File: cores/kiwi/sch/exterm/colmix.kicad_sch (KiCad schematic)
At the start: 9 parts

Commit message: issue#46
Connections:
- net H1B renamed H1_BUF
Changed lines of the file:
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@@
     (effects (font (size 1.27 1.27)) (justify right))
   )
-  (hierarchical_label "H1B" (shape input) (at 149.86 107.95 180)
+  (hierarchical_label "H1_BUF" (shape input) (at 149.86 107.95 180)
     (effects (font (size 1.27 1.27)) (justify right))
   )

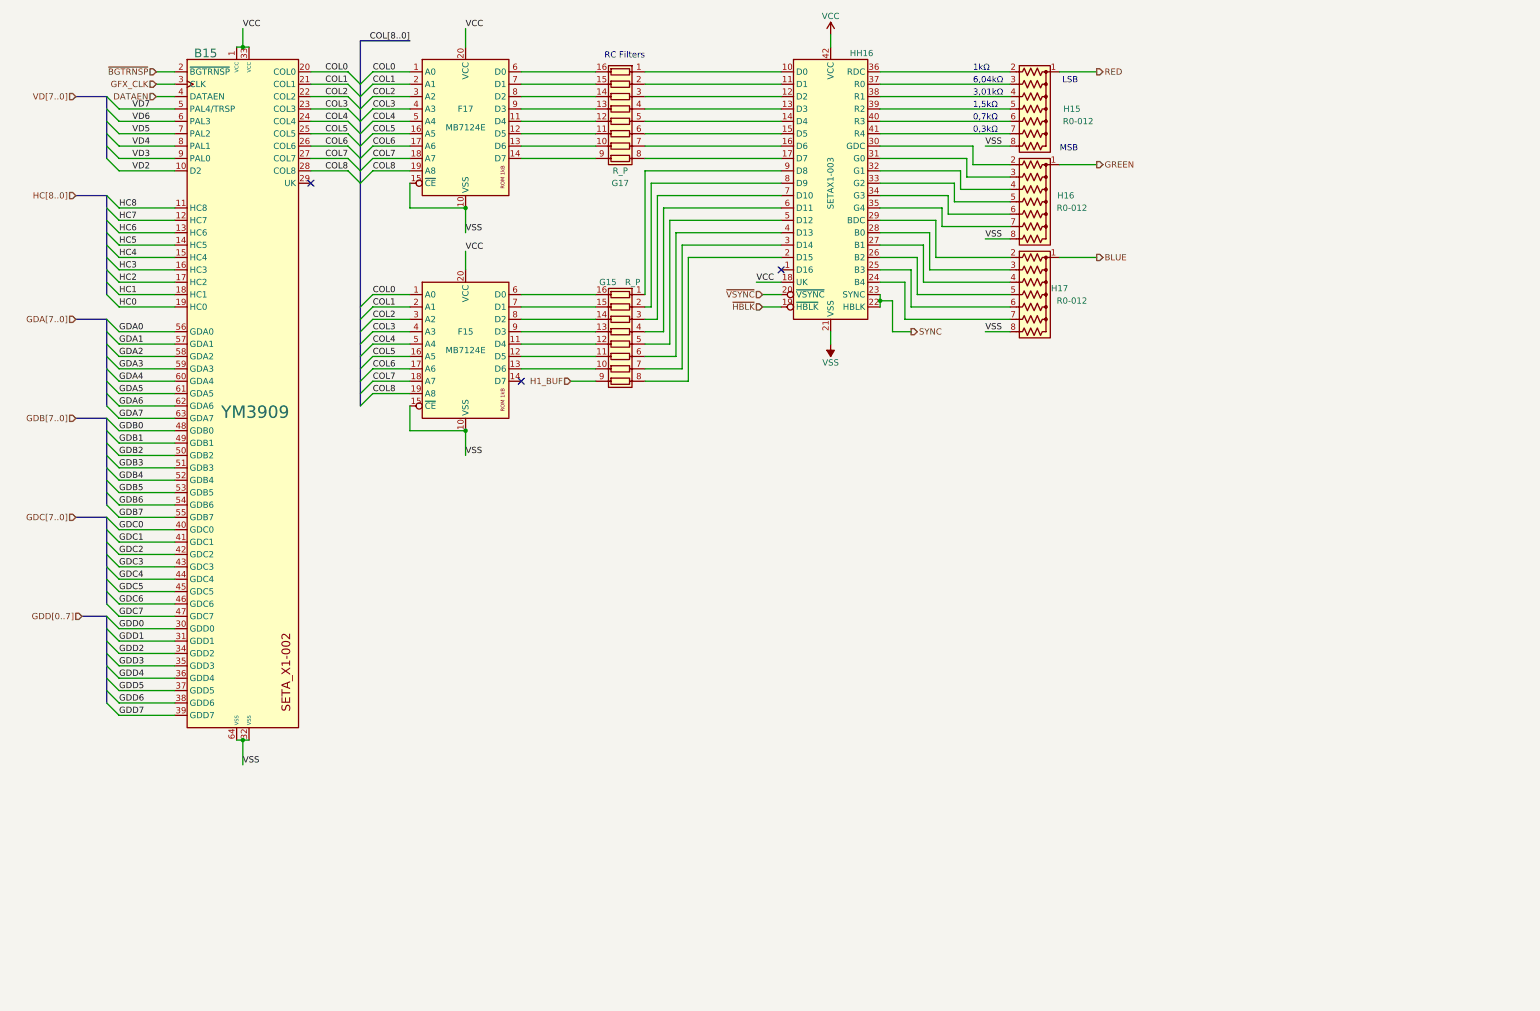
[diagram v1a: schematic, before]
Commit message: sheet_size_update
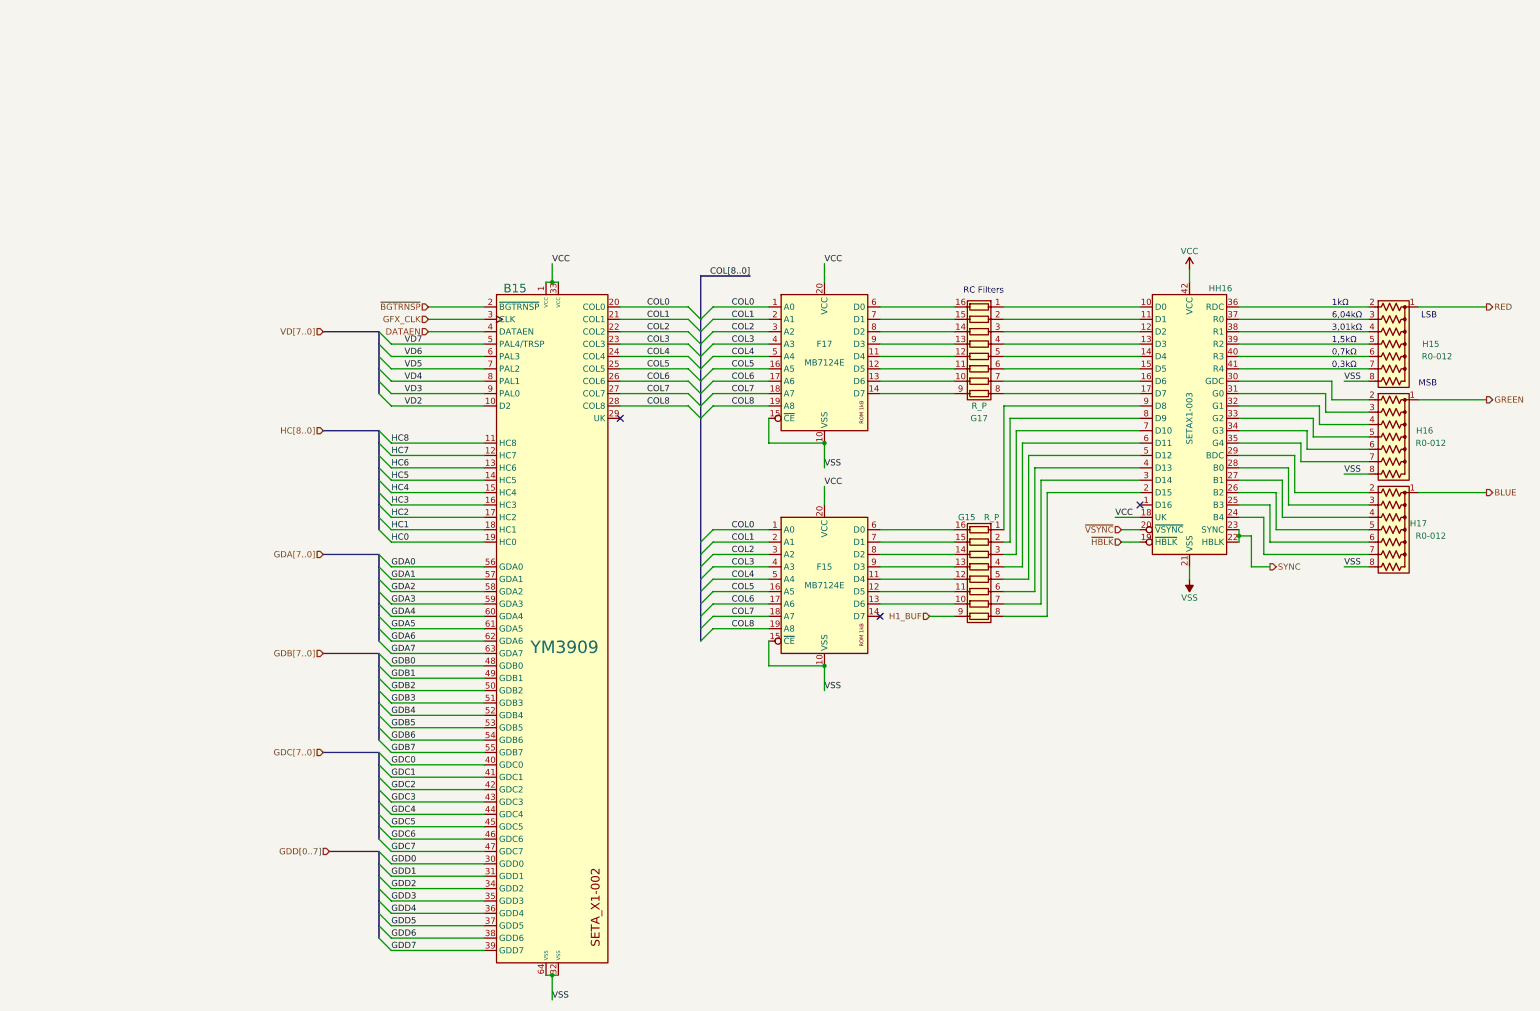
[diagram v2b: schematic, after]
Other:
- moved on the sheet: B15, F15, F17, G15, G17, H15, H16, H17, HH16
